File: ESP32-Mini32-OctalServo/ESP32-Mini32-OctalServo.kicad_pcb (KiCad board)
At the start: 2 copper layers, 66 x 91.4 mm, 44 parts, among them J101 + 5V Servo -, J102 Servo 1, J103 Servo 2, J104 Servo 3, J105 Servo 4, J106 Servo 5, J107 Servo 6, J108 Servo 7, J109 Servo 8, J301 RJ45, J302 RJ45, T301 - 15 in +, T302 - 15 out +, U101 74LV125AN, U102 74LV125AN, U201 TTGO-T7_S3-V1.1, U301 TCAN332DR, U401 AP63205

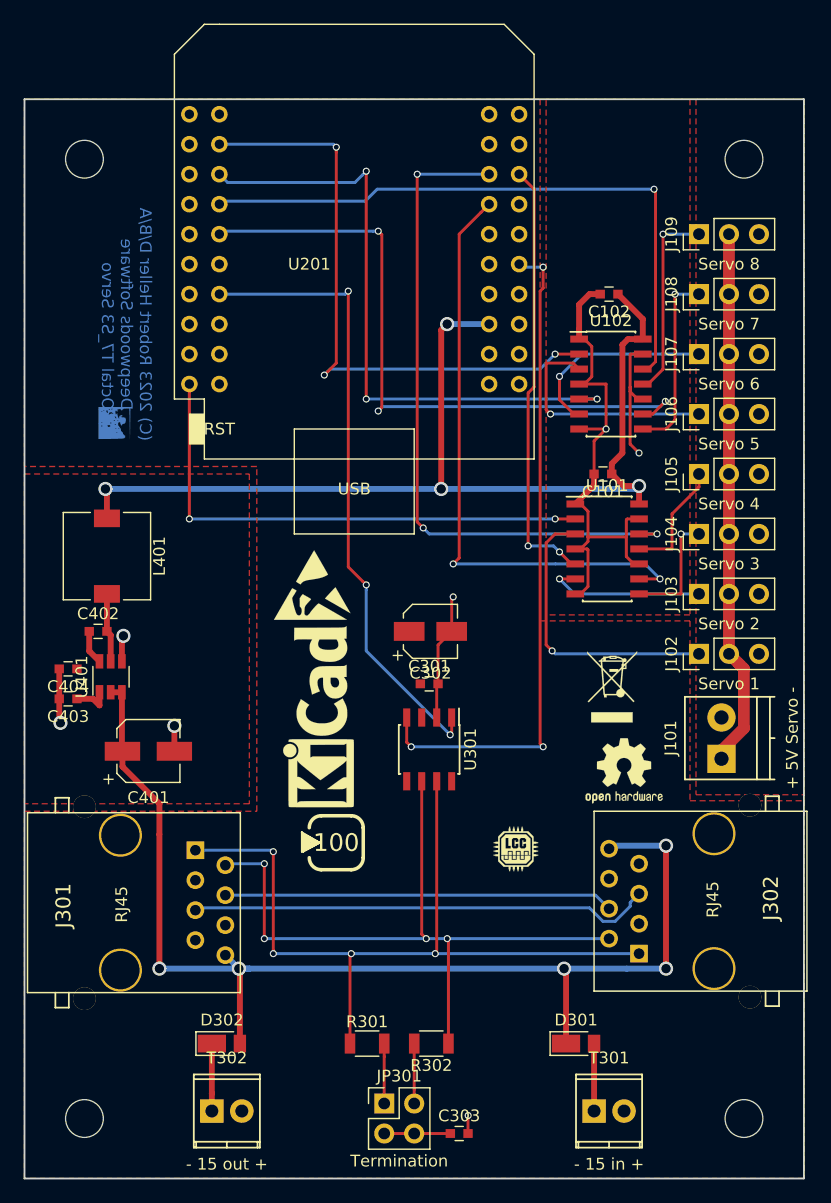
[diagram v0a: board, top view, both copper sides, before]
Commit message: Upgrade Kicad version.
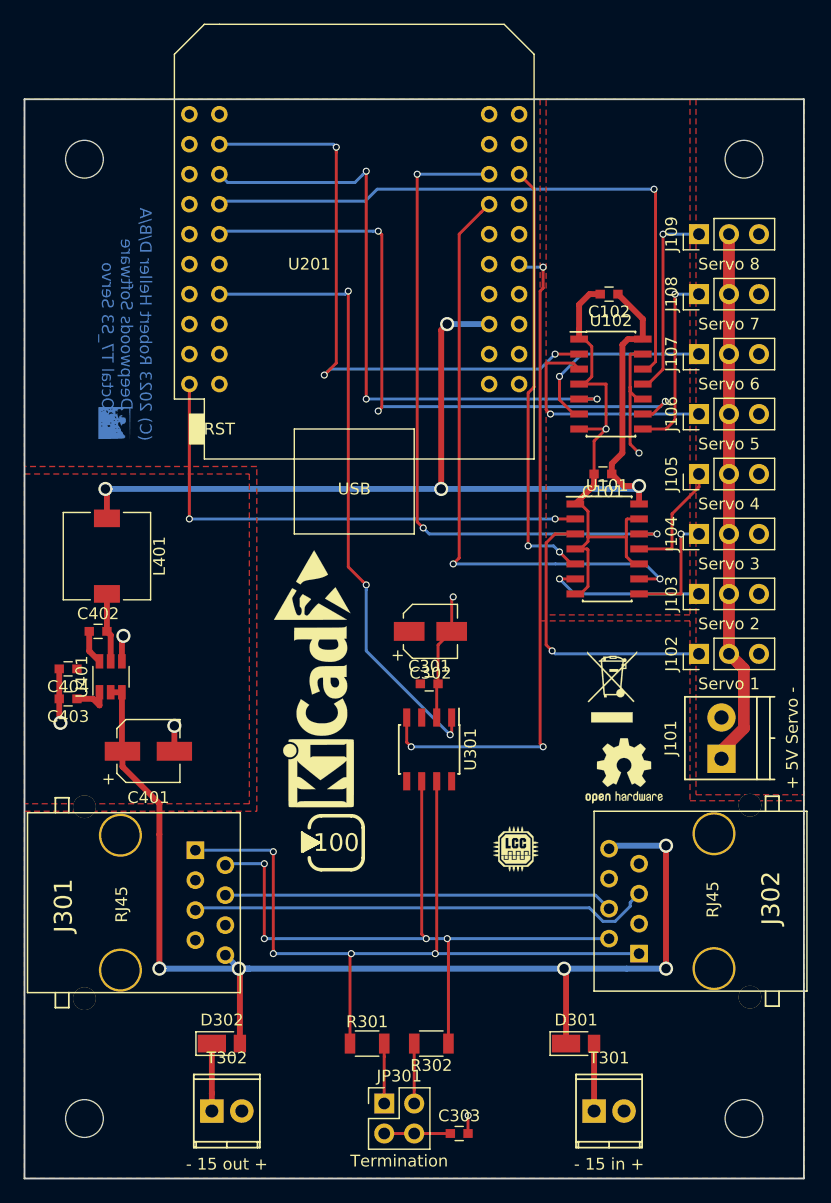
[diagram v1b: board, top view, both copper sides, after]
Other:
- net class Default removed
